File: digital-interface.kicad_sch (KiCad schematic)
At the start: 13 parts, among them U32001 Si8641BD-B-IS2, U32002 R05C05TE05S

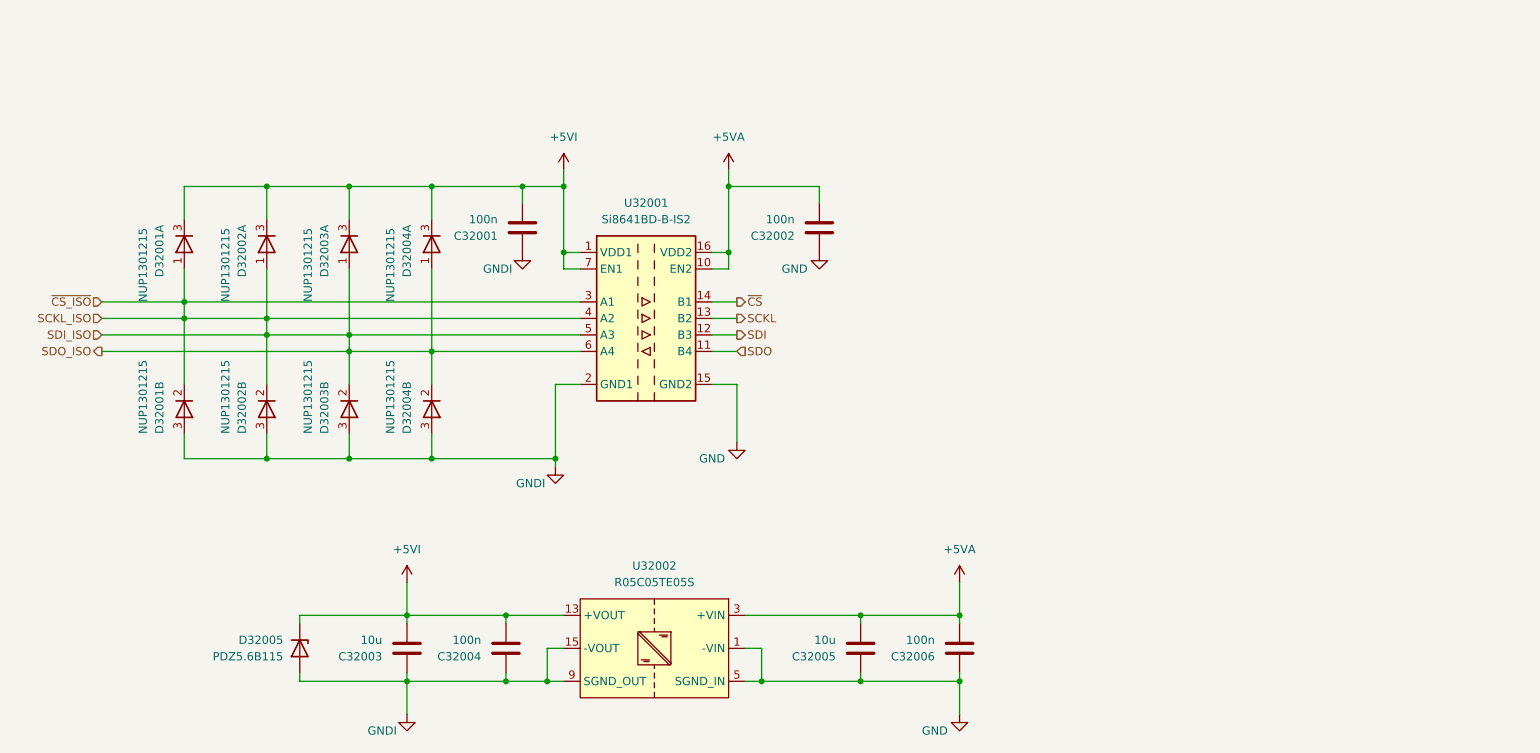
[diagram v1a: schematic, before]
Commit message: edit pss individual power nets for sub circuits
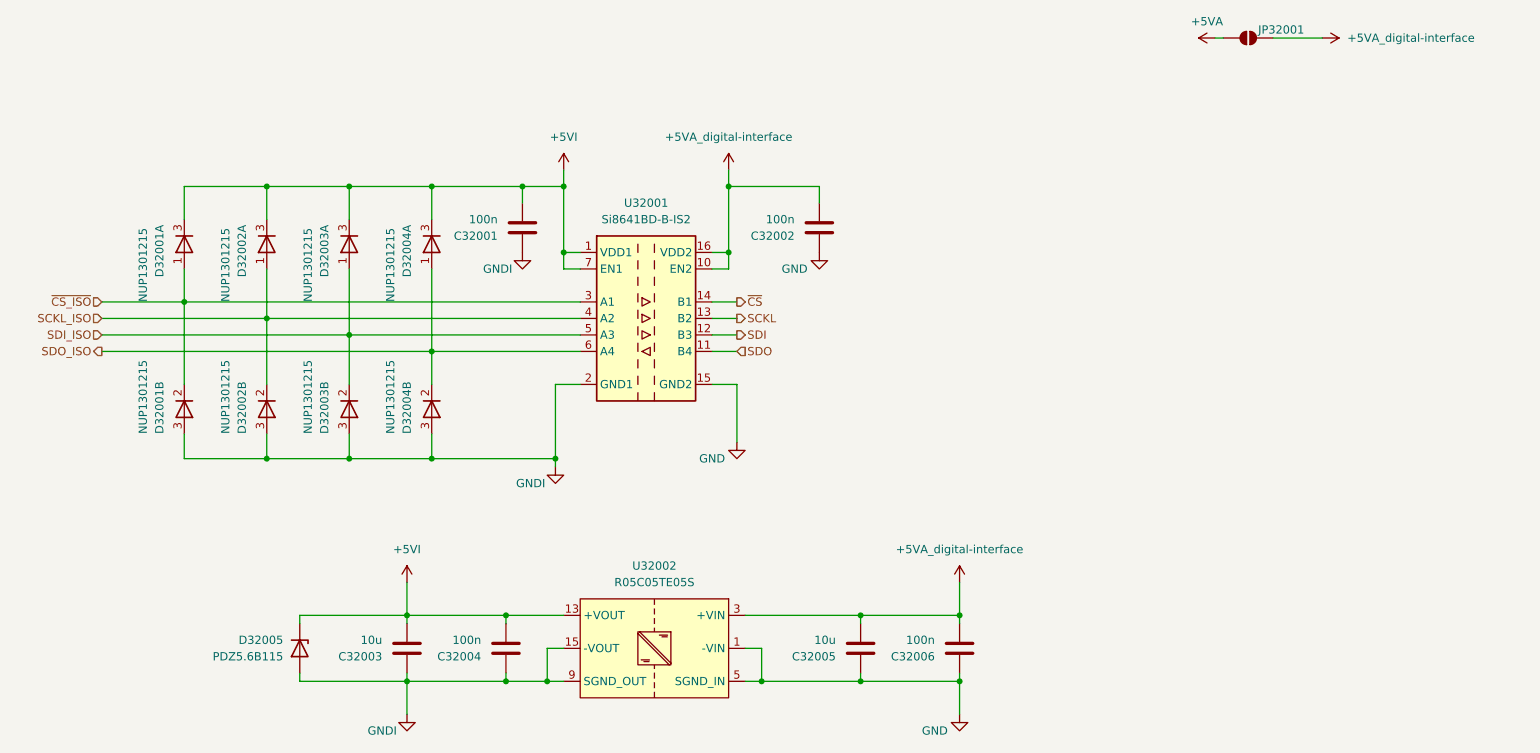
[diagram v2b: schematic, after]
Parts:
- added JP32001: SolderJumper_2_Open, symbol Jumper:SolderJumper_2_Open
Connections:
- net +5VA: now also JP32001.1 (A); no longer C32002.2, C32005.2, C32006.2, U32001.10 (EN2), U32001.16 (VDD2), U32002.3 (+VIN), U32002.4 (+VIN)
- net SCKL_ISO: no longer D32001.1 (A), D32001.2 (K), D32003.1 (A), D32003.2 (K), D32004.1 (A), D32004.2 (K), U32001.3 (A1), U32001.5 (A3), U32001.6 (A4)
- new net +5VA_digital-interface: C32002.2, C32005.2, C32006.2, JP32001.2 (B), U32001.10 (EN2), U32001.16 (VDD2), U32002.3 (+VIN), U32002.4 (+VIN)
- new net SDI_ISO: D32003.1 (A), D32003.2 (K), U32001.5 (A3)
- new net SDO_ISO: D32004.1 (A), D32004.2 (K), U32001.6 (A4)
- new net ~{CS_ISO}: D32001.1 (A), D32001.2 (K), U32001.3 (A1)

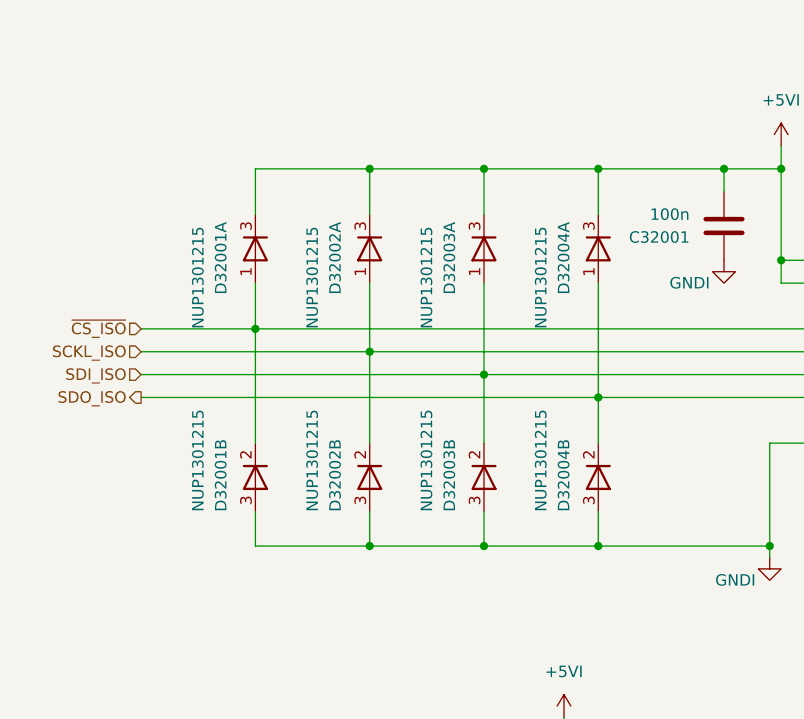
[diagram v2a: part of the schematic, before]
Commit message: fix digital-interface ERC error wrong connection of ESD diode pins
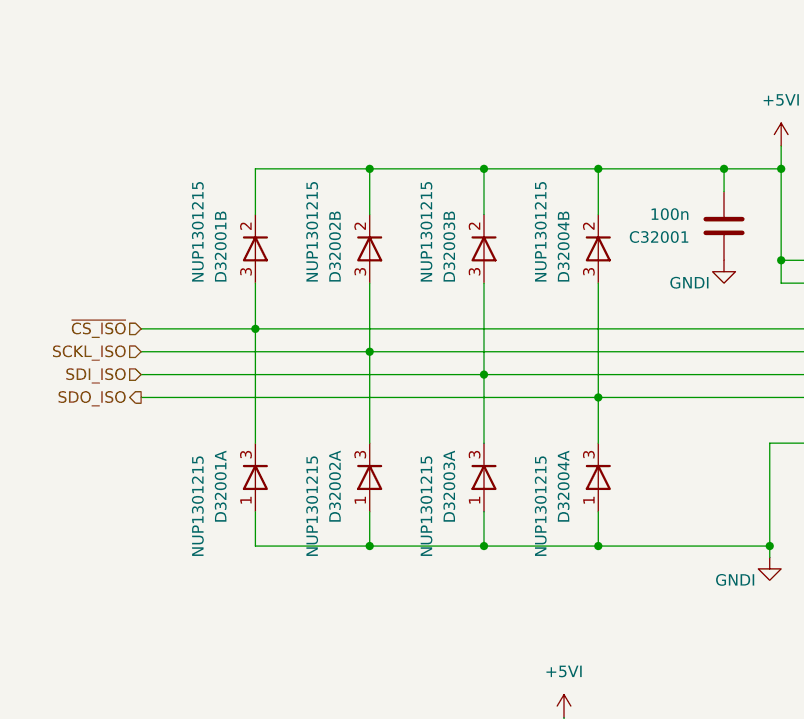
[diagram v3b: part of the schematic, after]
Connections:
- net +5VI: now also D32001.2 (K), D32002.2 (K), D32003.2 (K), D32004.2 (K); no longer D32001.3 (K), D32002.3 (K), D32003.3 (K), D32004.3 (K)
- net GNDI: now also D32001.1 (A), D32002.1 (A), D32003.1 (A), D32004.1 (A); no longer D32001.3 (K), D32002.3 (K), D32003.3 (K), D32004.3 (K)
- net SCKL_ISO: now also D32002.3 (K), D32002.3 (K); no longer D32002.1 (A), D32002.2 (K)
- net SDI_ISO: now also D32003.3 (K), D32003.3 (K); no longer D32003.1 (A), D32003.2 (K)
- net SDO_ISO: now also D32004.3 (K), D32004.3 (K); no longer D32004.1 (A), D32004.2 (K)
- net ~{CS_ISO}: now also D32001.3 (K), D32001.3 (K); no longer D32001.1 (A), D32001.2 (K)
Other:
- moved on the sheet: D32001A, D32001B, D32002A, D32002B, D32003A, D32003B, D32004A, D32004B
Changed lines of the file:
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@@
 	(symbol
 		(lib_id "Device:D_Dual_Series_AKC_Split")
-		(at 114.3 59.69 90)
+		(at 114.3 85.09 90)
 		(unit 1)
 		(exclude_from_sim no)
@@
 		(dnp no)
 		(property "Reference" "D32004"
-			(at 110.49 64.77 0)
+			(at 110.49 90.17 0)
 			(effects
 				(font
@@
 		)
 		(property "Value" "NUP1301215"
-			(at 107.95 68.58 0)
+			(at 107.95 93.98 0)
 			(effects
 				(font
@@
 		)
 		(property "Footprint" "Package_TO_SOT_SMD:SOT-23_Handsoldering"
-			(at 116.84 62.23 0)
+			(at 116.84 87.63 0)
 			(effects
 				(font
@@
 		)
 		(property "Datasheet" "https://assets.nexperia.com/documents/data-sheet/NUP1301.pdf"
-			(at 116.84 62.23 0)
+			(at 116.84 87.63 0)
 			(effects
 				(font
@@
 		)
 		(property "Description" "Dual diode, anode/cathode/center"
-			(at 114.3 59.69 0)
+			(at 114.3 85.09 0)
 			(effects
 				(font
@@
 		)
 		(property "MPN" "NUP1301,215"
-			(at 114.3 59.69 0)
+			(at 114.3 85.09 0)
 			(effects
 				(font
@@
 		)
 		(property "VPN" "771-NUP1301215"
-			(at 114.3 59.69 0)
+			(at 114.3 85.09 0)
 			(effects
 				(font
@@
 	(symbol
 		(lib_id "Device:D_Dual_Series_AKC_Split")
-		(at 76.2 85.09 270)
+		(at 76.2 59.69 270)
 		(unit 2)
 		(exclude_from_sim no)
@@
 		(dnp no)
 		(property "Reference" "D32001"
-			(at 72.39 88.9 0)
+			(at 72.39 63.5 0)
 			(effects
 				(font
@@
 		)
 		(property "Value" "NUP1301215"
-			(at 69.85 88.9 0)
+			(at 69.85 63.5 0)
 			(effects
 				(font
@@
 		)
 		(property "Footprint" "Package_TO_SOT_SMD:SOT-23_Handsoldering"
-			(at 73.66 82.55 0)
+			(at 73.66 57.15 0)
 			(effects
 				(font
@@
 		)
 		(property "Datasheet" "https://assets.nexperia.com/documents/data-sheet/NUP1301.pdf"
-			(at 73.66 82.55 0)
+			(at 73.66 57.15 0)
 			(effects
 				(font
@@
 		)
 		(property "Description" "Dual diode, anode/cathode/center"
-			(at 76.2 85.09 0)
+			(at 76.2 59.69 0)
 			(effects
 				(font
@@
 		)
 		(property "MPN" "NUP1301,215"
-			(at 76.2 85.09 0)
+			(at 76.2 59.69 0)
 			(effects
 				(font
@@
 		)
 		(property "VPN" "771-NUP1301215"
-			(at 76.2 85.09 0)
+			(at 76.2 59.69 0)
 			(effects
 				(font
@@
 	(symbol
 		(lib_id "Device:D_Dual_Series_AKC_Split")
-		(at 88.9 85.09 270)
+		(at 88.9 59.69 270)
 		(unit 2)
 		(exclude_from_sim no)
@@
 		(dnp no)
 		(property "Reference" "D32002"
-			(at 85.09 88.9 0)
+			(at 85.09 63.5 0)
 			(effects
 				(font
@@
 		)
 		(property "Value" "NUP1301215"
-			(at 82.55 88.9 0)
+			(at 82.55 63.5 0)
 			(effects
 				(font
@@
 		)
 		(property "Footprint" "Package_TO_SOT_SMD:SOT-23_Handsoldering"
-			(at 86.36 82.55 0)
+			(at 86.36 57.15 0)
 			(effects
 				(font
@@
 		)
 		(property "Datasheet" "https://assets.nexperia.com/documents/data-sheet/NUP1301.pdf"
-			(at 86.36 82.55 0)
+			(at 86.36 57.15 0)
 			(effects
 				(font
@@
 		)
 		(property "Description" "Dual diode, anode/cathode/center"
-			(at 88.9 85.09 0)
+			(at 88.9 59.69 0)
 			(effects
 				(font
@@
 		)
 		(property "MPN" "NUP1301,215"
-			(at 88.9 85.09 0)
+			(at 88.9 59.69 0)
 			(effects
 				(font
@@
 		)
 		(property "VPN" "771-NUP1301215"
-			(at 88.9 85.09 0)
+			(at 88.9 59.69 0)
 			(effects
 				(font
@@
 	(symbol
 		(lib_id "Device:D_Dual_Series_AKC_Split")
-		(at 114.3 85.09 270)
+		(at 114.3 59.69 270)
 		(unit 2)
 		(exclude_from_sim no)
@@
 		(dnp no)
 		(property "Reference" "D32004"
-			(at 110.49 88.9 0)
+			(at 110.49 63.5 0)
 			(effects
 				(font
@@
 		)
 		(property "Value" "NUP1301215"
-			(at 107.95 88.9 0)
+			(at 107.95 63.5 0)
 			(effects
 				(font
@@
 		)
 		(property "Footprint" "Package_TO_SOT_SMD:SOT-23_Handsoldering"
-			(at 111.76 82.55 0)
+			(at 111.76 57.15 0)
 			(effects
 				(font
@@
 		)
 		(property "Datasheet" "https://assets.nexperia.com/documents/data-sheet/NUP1301.pdf"
-			(at 111.76 82.55 0)
+			(at 111.76 57.15 0)
 			(effects
 				(font
@@
 		)
 		(property "Description" "Dual diode, anode/cathode/center"
-			(at 114.3 85.09 0)
+			(at 114.3 59.69 0)
 			(effects
 				(font
@@
 		)
 		(property "MPN" "NUP1301,215"
-			(at 114.3 85.09 0)
+			(at 114.3 59.69 0)
 			(effects
 				(font
@@
 		)
 		(property "VPN" "771-NUP1301215"
-			(at 114.3 85.09 0)
+			(at 114.3 59.69 0)
 			(effects
 				(font
@@
 	(symbol
 		(lib_id "Device:D_Dual_Series_AKC_Split")
-		(at 88.9 59.69 90)
+		(at 88.9 85.09 90)
 		(unit 1)
 		(exclude_from_sim no)
@@
 		(dnp no)
 		(property "Reference" "D32002"
-			(at 85.09 64.77 0)
+			(at 85.09 90.17 0)
 			(effects
 				(font
@@
 		)
 		(property "Value" "NUP1301215"
-			(at 82.55 68.58 0)
+			(at 82.55 93.98 0)
 			(effects
 				(font
@@
 		)
 		(property "Footprint" "Package_TO_SOT_SMD:SOT-23_Handsoldering"
-			(at 91.44 62.23 0)
+			(at 91.44 87.63 0)
 			(effects
 				(font
@@
 		)
 		(property "Datasheet" "https://assets.nexperia.com/documents/data-sheet/NUP1301.pdf"
-			(at 91.44 62.23 0)
+			(at 91.44 87.63 0)
 			(effects
 				(font
@@
 		)
 		(property "Description" "Dual diode, anode/cathode/center"
-			(at 88.9 59.69 0)
+			(at 88.9 85.09 0)
 			(effects
 				(font
@@
 		)
 		(property "MPN" "NUP1301,215"
-			(at 88.9 59.69 0)
+			(at 88.9 85.09 0)
 			(effects
 				(font
@@
 		)
 		(property "VPN" "771-NUP1301215"
-			(at 88.9 59.69 0)
+			(at 88.9 85.09 0)
 			(effects
 				(font
@@
 	(symbol
 		(lib_id "Device:D_Dual_Series_AKC_Split")
-		(at 101.6 59.69 90)
+		(at 101.6 85.09 90)
 		(unit 1)
 		(exclude_from_sim no)
@@
 		(dnp no)
 		(property "Reference" "D32003"
-			(at 97.79 64.77 0)
+			(at 97.79 90.17 0)
 			(effects
 				(font
@@
 		)
 		(property "Value" "NUP1301215"
-			(at 95.25 68.58 0)
+			(at 95.25 93.98 0)
 			(effects
 				(font
@@
 		)
 		(property "Footprint" "Package_TO_SOT_SMD:SOT-23_Handsoldering"
-			(at 104.14 62.23 0)
+			(at 104.14 87.63 0)
 			(effects
 				(font
@@
 		)
 		(property "Datasheet" "https://assets.nexperia.com/documents/data-sheet/NUP1301.pdf"
-			(at 104.14 62.23 0)
+			(at 104.14 87.63 0)
 			(effects
 				(font
@@
 		)
 		(property "Description" "Dual diode, anode/cathode/center"
-			(at 101.6 59.69 0)
+			(at 101.6 85.09 0)
 			(effects
 				(font
@@
 		)
 		(property "MPN" "NUP1301,215"
-			(at 101.6 59.69 0)
+			(at 101.6 85.09 0)
 			(effects
 				(font
@@
 		)
 		(property "VPN" "771-NUP1301215"
-			(at 101.6 59.69 0)
+			(at 101.6 85.09 0)
 			(effects
 				(font
@@
 	(symbol
 		(lib_id "Device:D_Dual_Series_AKC_Split")
-		(at 76.2 59.69 90)
+		(at 76.2 85.09 90)
 		(unit 1)
 		(exclude_from_sim no)
@@
 		(dnp no)
 		(property "Reference" "D32001"
-			(at 72.39 64.77 0)
+			(at 72.39 90.17 0)
 			(effects
 				(font
@@
 		)
 		(property "Value" "NUP1301215"
-			(at 69.85 68.58 0)
+			(at 69.85 93.98 0)
 			(effects
 				(font
@@
 		)
 		(property "Footprint" "Package_TO_SOT_SMD:SOT-23_Handsoldering"
-			(at 78.74 62.23 0)
+			(at 78.74 87.63 0)
 			(effects
 				(font
@@
 		)
 		(property "Datasheet" "https://assets.nexperia.com/documents/data-sheet/NUP1301.pdf"
-			(at 78.74 62.23 0)
+			(at 78.74 87.63 0)
 			(effects
 				(font
@@
 		)
 		(property "Description" "Dual diode, anode/cathode/center"
-			(at 76.2 59.69 0)
+			(at 76.2 85.09 0)
 			(effects
 				(font
@@
 		)
 		(property "MPN" "NUP1301,215"
-			(at 76.2 59.69 0)
+			(at 76.2 85.09 0)
 			(effects
 				(font
@@
 		)
 		(property "VPN" "771-NUP1301215"
-			(at 76.2 59.69 0)
+			(at 76.2 85.09 0)
 			(effects
 				(font
@@
 	(symbol
 		(lib_id "Device:D_Dual_Series_AKC_Split")
-		(at 101.6 85.09 270)
+		(at 101.6 59.69 270)
 		(unit 2)
 		(exclude_from_sim no)
@@
 		(dnp no)
 		(property "Reference" "D32003"
-			(at 97.79 88.9 0)
+			(at 97.79 63.5 0)
 			(effects
 				(font
@@
 		)
 		(property "Value" "NUP1301215"
-			(at 95.25 88.9 0)
+			(at 95.25 63.5 0)
 			(effects
 				(font
@@
 		)
 		(property "Footprint" "Package_TO_SOT_SMD:SOT-23_Handsoldering"
-			(at 99.06 82.55 0)
+			(at 99.06 57.15 0)
 			(effects
 				(font
@@
 		)
 		(property "Datasheet" "https://assets.nexperia.com/documents/data-sheet/NUP1301.pdf"
-			(at 99.06 82.55 0)
+			(at 99.06 57.15 0)
 			(effects
 				(font
@@
 		)
 		(property "Description" "Dual diode, anode/cathode/center"
-			(at 101.6 85.09 0)
+			(at 101.6 59.69 0)
 			(effects
 				(font
@@
 		)
 		(property "MPN" "NUP1301,215"
-			(at 101.6 85.09 0)
+			(at 101.6 59.69 0)
 			(effects
 				(font
@@
 		)
 		(property "VPN" "771-NUP1301215"
-			(at 101.6 85.09 0)
-			(effects
-				(font
+			(at 101.6 59.69 0)
+			(effects
+				(font

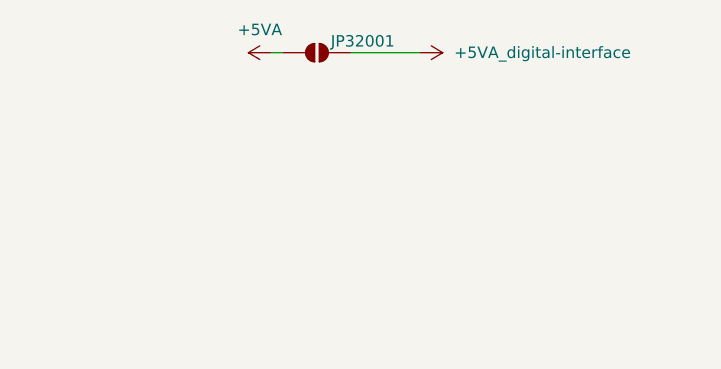
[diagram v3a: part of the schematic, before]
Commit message: fix pss ERC error: missing power flag
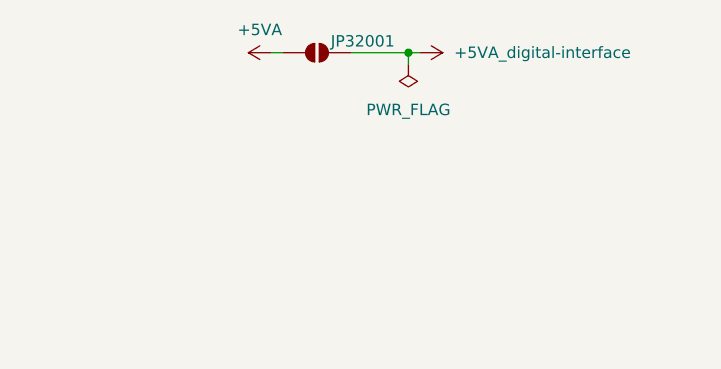
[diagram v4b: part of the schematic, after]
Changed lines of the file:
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@@
+	)
+	(junction
+		(at 250.19 27.94)
+		(diameter 0)
+		(color 0 0 0 0)
 	)
 	(junction
@@
 	(wire
 		(pts
-			(xy 251.46 27.94) (xy 243.84 27.94)
+			(xy 251.46 27.94) (xy 250.19 27.94)
 		)
 		(stroke
@@
 	(wire
 		(pts
+			(xy 250.19 27.94) (xy 243.84 27.94)
+		)
+		(stroke
+			(width 0)
+			(type default)
+		)
+	)
+	(wire
+		(pts
 			(xy 101.6 92.71) (xy 101.6 88.9)
 		)
@@
 		(pts
 			(xy 114.3 76.2) (xy 114.3 81.28)
+		)
+		(stroke
+			(width 0)
+			(type default)
+		)
+	)
+	(wire
+		(pts
+			(xy 250.19 29.21) (xy 250.19 27.94)
 		)
 		(stroke
@@
 					(unit 1)
 				)
+			)
+		)
+	)
+	(symbol
+		(lib_id "pss:PWR_FLAG")
+		(at 250.19 29.21 180)
+		(unit 1)
+		(exclude_from_sim no)
+		(in_bom yes)
+		(on_board yes)
+		(dnp no)
+		(fields_autoplaced yes)
+		(property "Reference" "#FLG032001"
+			(at 250.19 31.115 0)
+			(effects
+				(font
+					(size 1.27 1.27)
+				)
+				(hide yes)
+			)
+		)
+		(property "Value" "PWR_FLAG"
+			(at 250.19 34.29 0)
+			(effects
+				(font
+					(size 1.27 1.27)
+				)
+			)
+		)
+		(property "Footprint" ""
+			(at 250.19 29.21 0)
+			(effects
+				(font
+					(size 1.27 1.27)
+				)
+				(hide yes)
+			)
+		)
+		(property "Datasheet" "~"
+			(at 250.19 29.21 0)
+			(effects
+				(font
+					(size 1.27 1.27)
+				)
+				(hide yes)
+			)
+		)
+		(property "Description" "Special symbol for telling ERC where power comes from"
+			(at 250.19 29.21 0)
+			(effects
+				(font
+					(size 1.27 1.27)
+				)
+				(hide yes)
+			)
+		)
+		(pin "1"
+		)
+		(instances
+			(project "pss"
+				(path "/3c438cf7-9350-4e9f-8115-1deba8984176/07c1abbb-a625-4c44-bef8-8e7c07c13d28"
+					(reference "#FLG032001")
+					(unit 1)
+				)

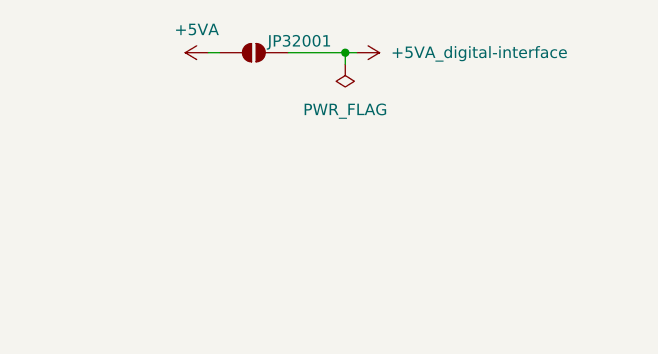
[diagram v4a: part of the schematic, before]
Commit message: fix pss ERC errors: multiple outputs connected
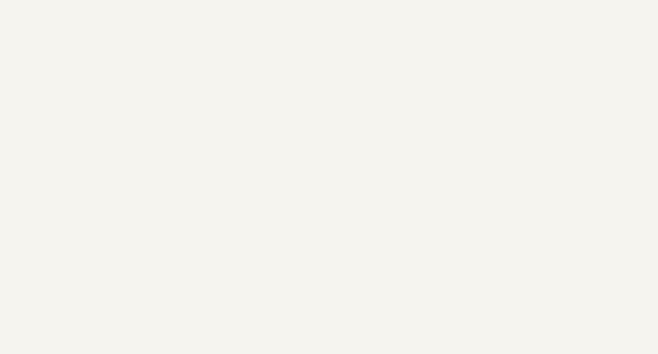
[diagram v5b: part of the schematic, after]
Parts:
- removed JP32001: SolderJumper_2_Open, symbol Jumper:SolderJumper_2_Open
